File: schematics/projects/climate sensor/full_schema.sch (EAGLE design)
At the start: 42 parts, among them Q1 2N3906BU, Q2 2N3906BU, Q3 2N3906BU, Q4 2N3904, Q5 2N3904

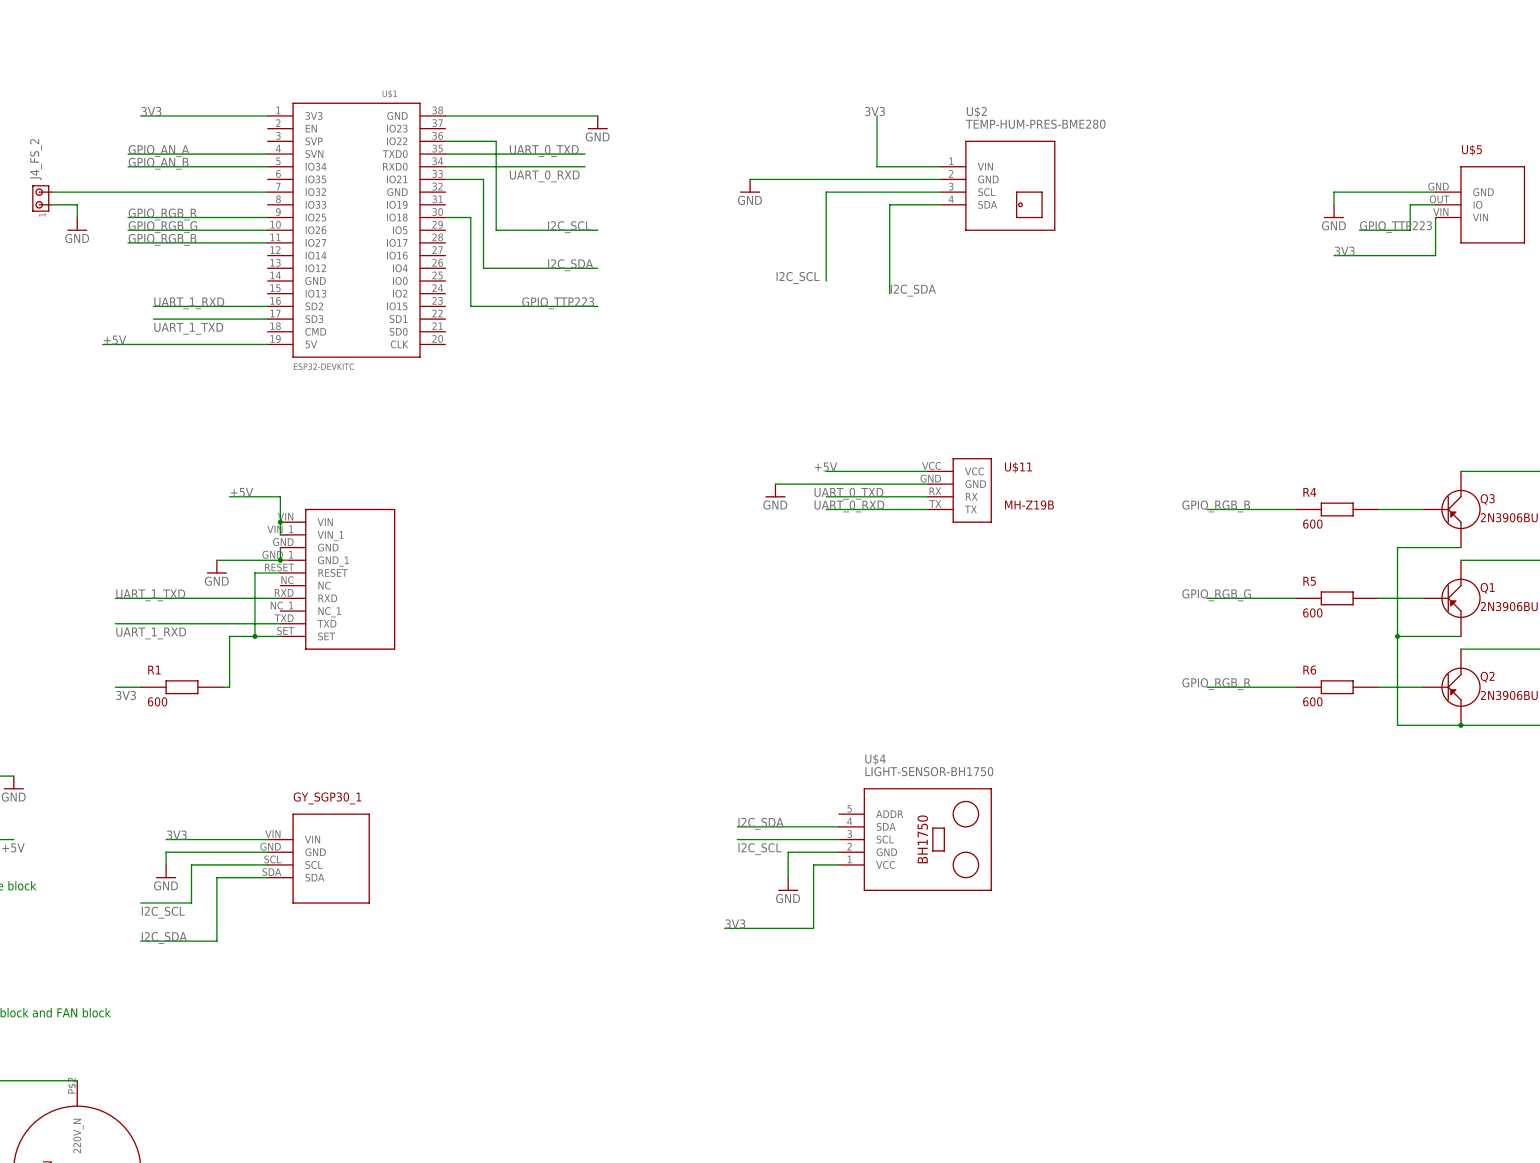
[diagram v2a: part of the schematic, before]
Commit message: added IR interface
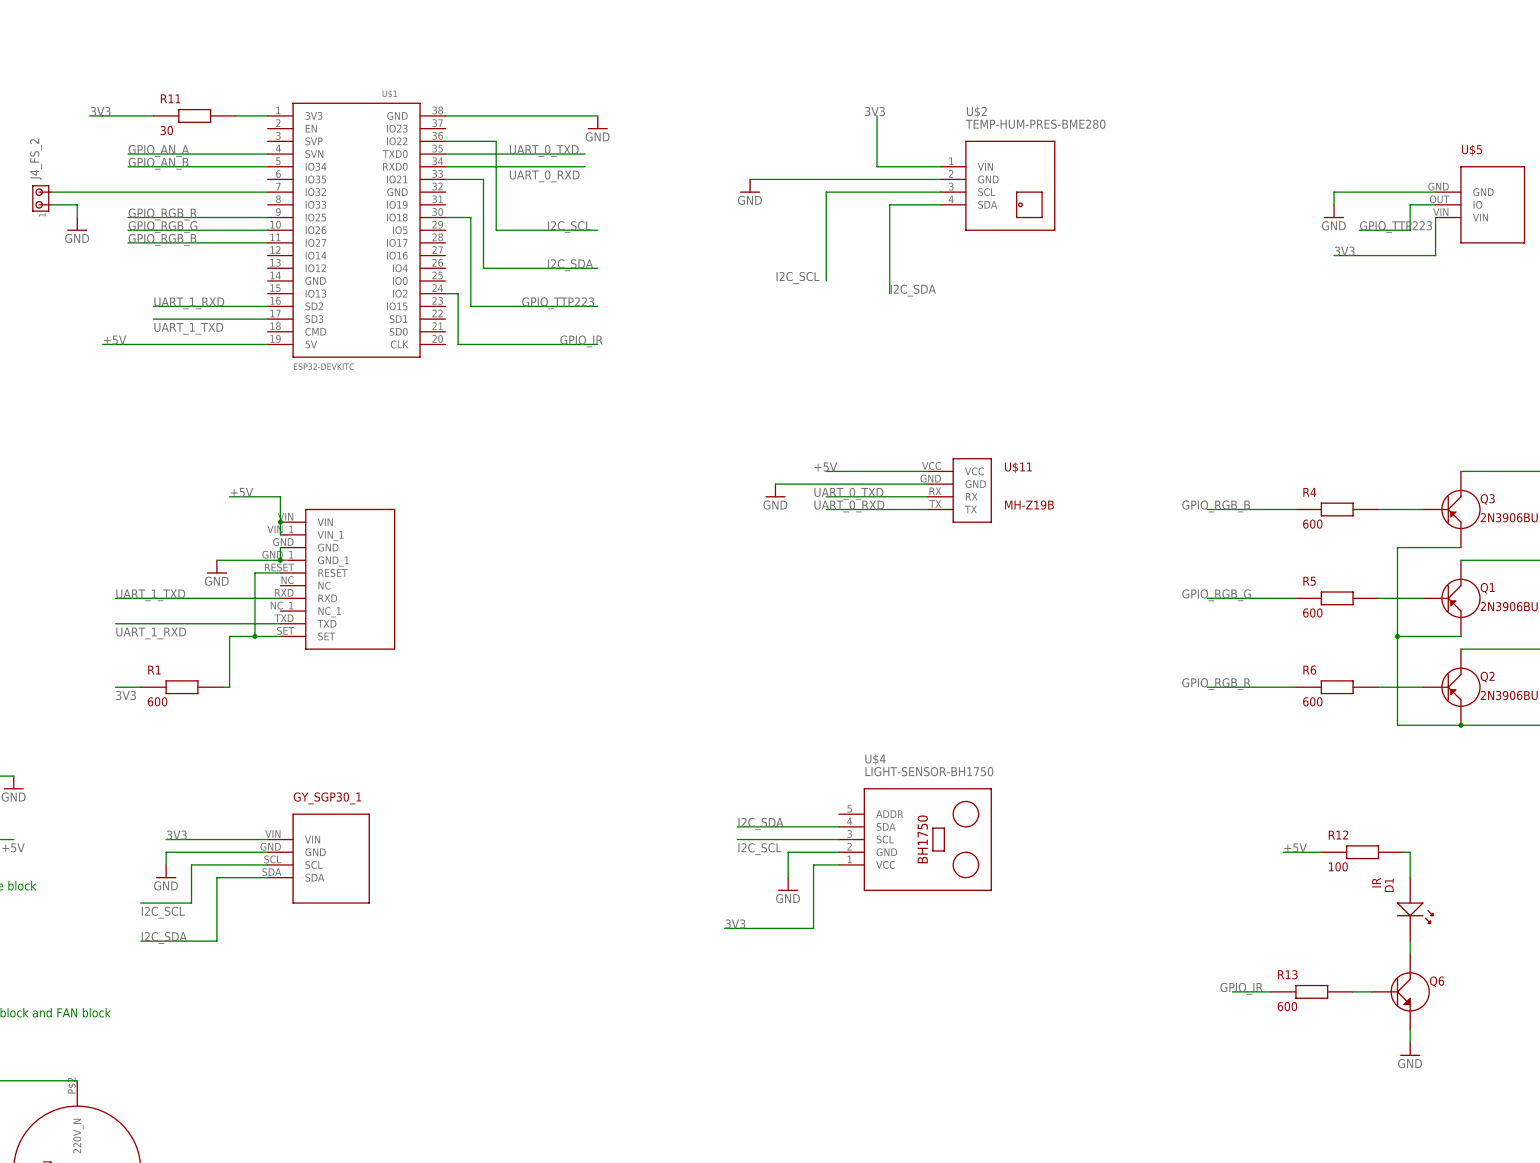
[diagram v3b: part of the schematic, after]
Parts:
- added D1: IR, my_devices:LD
- added Q6: (no value), my_devices:TRANSISTOR_NPN
- added R11: 30, my_devices:R
- added R12: 100, my_devices:R
- added R13: 600, my_devices:R
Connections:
- new net GPIO_IR: R13.P$1, U$1.IO2
- new net N$24: R11.P$2, U$1.3V3
- new net N$25: D1.P$2, Q6.C
- new net N$26: D1.P$1, R12.P$2
- new net N$27: Q6.B, R13.P$2
- net +5V: now also R12.P$1
- net 3V3: now also R11.P$1; no longer U$1.3V3
- net GND: now also Q6.E
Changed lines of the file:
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@@
 <schematic_group name="5V_SUPPLY_JET"/>
 <schematic_group name="FAN"/>
+<schematic_group name="IR"/>
 </groups>
 <parts>
@@
 <part name="R9" library="my_devices" deviceset="R" device="" value="600"/>
 <part name="R10" library="my_devices" deviceset="R" device="" value="600"/>
+<part name="R11" library="my_devices" deviceset="R" device="" value="30"/>
+<part name="D1" library="my_devices" deviceset="LD" device="" value="IR"/>
+<part name="GND10" library="supply1" library_urn="urn:adsk.eagle:library:371" deviceset="GND" device=""/>
+<part name="Q6" library="my_devices" deviceset="TRANSISTOR_NPN" device=""/>
+<part name="R12" library="my_devices" deviceset="R" device="" value="100"/>
+<part name="R13" library="my_devices" deviceset="R" device="" value="600"/>
 </parts>
 <sheets>
@@
 <attribute name="VALUE" x="-232.41" y="118.11" size="1.778" layer="94"/>
 </instance>
+<instance part="R11" gate="G$1" x="-71.12" y="104.14" smashed="yes">
+<attribute name="NAME" x="-77.47" y="106.68" size="1.778" layer="94"/>
+<attribute name="VALUE" x="-77.47" y="100.33" size="1.778" layer="94"/>
+</instance>
+<instance part="D1" gate="G$1" x="172.72" y="-55.88" smashed="yes" rot="R270" grouprefs="IR">
+<attribute name="NAME" x="167.64" y="-48.26" size="1.778" layer="94" rot="R270"/>
+<attribute name="VALUE" x="165.1" y="-48.26" size="1.778" layer="94" rot="R270"/>
+</instance>
+<instance part="GND10" gate="1" x="172.72" y="-83.82" smashed="yes" grouprefs="IR">
+<attribute name="VALUE" x="170.18" y="-86.36" size="1.778" layer="96"/>
+</instance>
+<instance part="Q6" gate="G$1" x="172.72" y="-71.12" smashed="yes" grouprefs="IR">
+<attribute name="NAME" x="176.53" y="-69.85" size="1.778" layer="94"/>
+<attribute name="VALUE" x="176.53" y="-73.66" size="1.778" layer="94"/>
+</instance>
+<instance part="R12" gate="G$1" x="162.56" y="-43.18" smashed="yes" grouprefs="IR">
+<attribute name="NAME" x="156.21" y="-40.64" size="1.778" layer="94"/>
+<attribute name="VALUE" x="156.21" y="-46.99" size="1.778" layer="94"/>
+</instance>
+<instance part="R13" gate="G$1" x="152.4" y="-71.12" smashed="yes" grouprefs="IR">
+<attribute name="NAME" x="146.05" y="-68.58" size="1.778" layer="94"/>
+<attribute name="VALUE" x="146.05" y="-74.93" size="1.778" layer="94"/>
+</instance>
 </instances>
 <busses>
@@
 <pinref part="GND3" gate="1" pin="GND"/>
 <wire x1="-299.72" y1="149.86" x2="-243.84" y2="149.86" width="0.1524" layer="91"/>
+</segment>
+<segment>
+<pinref part="Q6" gate="G$1" pin="E"/>
+<pinref part="GND10" gate="1" pin="GND"/>
+<wire x1="172.72" y1="-78.74" x2="172.72" y2="-81.28" width="0.1524" layer="91" grouprefs="IR"/>
 </segment>
 </net>
@@
 <label x="-210.82" y="121.92" size="1.778" layer="95"/>
 </segment>
+<segment>
+<pinref part="R12" gate="G$1" pin="P$1"/>
+<wire x1="154.94" y1="-43.18" x2="147.32" y2="-43.18" width="0.1524" layer="91" grouprefs="IR"/>
+<label x="147.32" y="-43.18" size="1.778" layer="95" grouprefs="IR"/>
+</segment>
 </net>
 <net name="3V3" class="0">
-<segment>
-<pinref part="U$1" gate="G$1" pin="3V3"/>
-<wire x1="-55.88" y1="104.14" x2="-81.28" y2="104.14" width="0.1524" layer="91" grouprefs="ESP"/>
-<label x="-81.28" y="104.14" size="1.778" layer="95" grouprefs="ESP"/>
-</segment>
 <segment>
 <pinref part="U$2" gate="G$1" pin="VIN"/>
@@
 <junction x="-218.44" y="104.14"/>
 <label x="-203.2" y="104.14" size="1.778" layer="95"/>
+</segment>
+<segment>
+<pinref part="R11" gate="G$1" pin="P$1"/>
+<wire x1="-78.74" y1="104.14" x2="-88.9" y2="104.14" width="0.1524" layer="91"/>
+<wire x1="-91.44" y1="104.14" x2="-88.9" y2="104.14" width="0.1524" layer="91"/>
+<label x="-91.44" y="104.14" size="1.778" layer="95"/>
 </segment>
 </net>
@@
 </segment>
 </net>
+<net name="N$24" class="0">
+<segment>
+<pinref part="U$1" gate="G$1" pin="3V3"/>
+<pinref part="R11" gate="G$1" pin="P$2"/>
+<wire x1="-55.88" y1="104.14" x2="-62.23" y2="104.14" width="0.1524" layer="91"/>
+</segment>
+</net>
+<net name="N$25" class="0">
+<segment>
+<pinref part="D1" gate="G$1" pin="P$2"/>
+<pinref part="Q6" gate="G$1" pin="C"/>
+<wire x1="172.72" y1="-60.96" x2="172.72" y2="-63.5" width="0.1524" layer="91" grouprefs="IR"/>
+</segment>
+</net>
+<net name="N$26" class="0">
+<segment>
+<pinref part="R12" gate="G$1" pin="P$2"/>
+<wire x1="171.45" y1="-43.18" x2="172.72" y2="-43.18" width="0.1524" layer="91" grouprefs="IR"/>
+<pinref part="D1" gate="G$1" pin="P$1"/>
+<wire x1="172.72" y1="-43.18" x2="172.72" y2="-48.26" width="0.1524" layer="91" grouprefs="IR"/>
+</segment>
+</net>
+<net name="N$27" class="0">
+<segment>
+<pinref part="Q6" gate="G$1" pin="B"/>
+<pinref part="R13" gate="G$1" pin="P$2"/>
+<wire x1="165.1" y1="-71.12" x2="161.29" y2="-71.12" width="0.1524" layer="91" grouprefs="IR"/>
+</segment>
+</net>
+<net name="GPIO_IR" class="0">
+<segment>
+<pinref part="R13" gate="G$1" pin="P$1"/>
+<wire x1="144.78" y1="-71.12" x2="137.16" y2="-71.12" width="0.1524" layer="91" grouprefs="IR"/>
+<label x="134.62" y="-71.12" size="1.778" layer="95" grouprefs="IR"/>
+</segment>
+<segment>
+<pinref part="U$1" gate="G$1" pin="IO2"/>
+<wire x1="-20.32" y1="68.58" x2="-17.78" y2="68.58" width="0.1524" layer="91"/>
+<wire x1="-17.78" y1="68.58" x2="-17.78" y2="58.42" width="0.1524" layer="91"/>
+<wire x1="-17.78" y1="58.42" x2="10.16" y2="58.42" width="0.1524" layer="91"/>
+<label x="2.54" y="58.42" size="1.778" layer="95"/>
+</segment>
+</net>
